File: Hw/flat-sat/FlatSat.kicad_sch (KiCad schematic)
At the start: 84 parts, among them J1 Antenna, J2 Antenna, J3 periphs, J4 SWD, P1 USB_C_Plug_USB2.0, U1 TLV75733PDBVR, U10 LIS2DH, U11 BME280 /BMP280, U2 0900FM15D0039, U3 PE42421, U4 SX1262IMLTRT, U5 W25Q16JV, U6 0900FM15D0039, U7 PE42421, U8 SX1262IMLTRT, U9 RP2040, Y1 32Mhz, Y2 32Mhz, Y3 12MHz

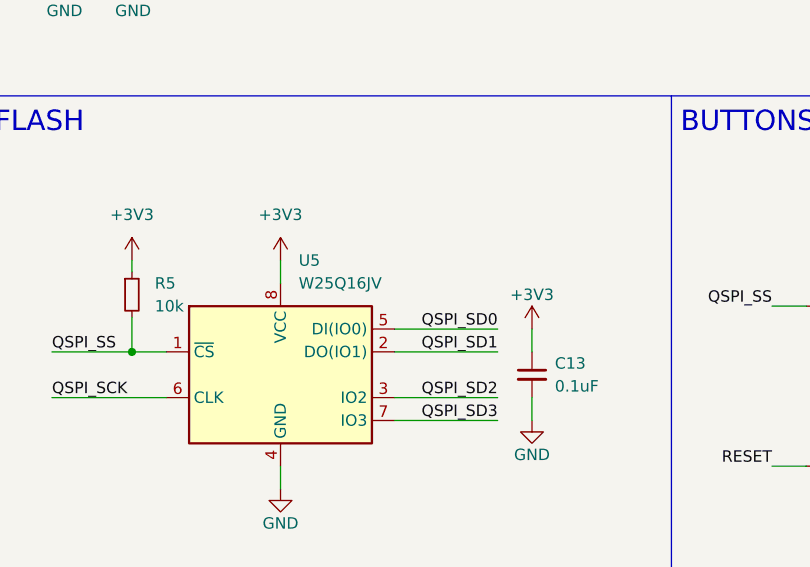
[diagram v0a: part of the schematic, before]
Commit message: feat(Hw):Update_Bom
#part memory flash updated
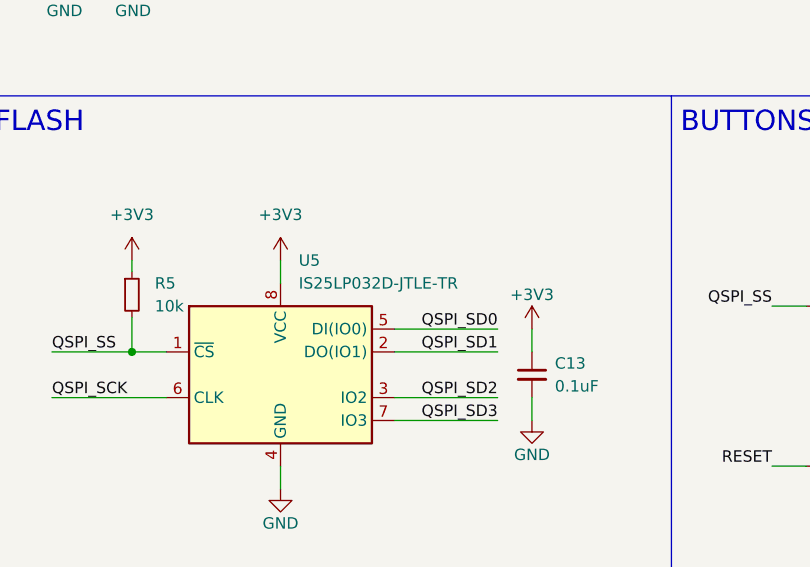
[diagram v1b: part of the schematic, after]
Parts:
- U5: value W25Q16JV -> IS25LP032D-JTLE-TR; LCSC# C571259 -> C5119926; Mouser# 454-W25Q16JVUUIQTR -> (none); manf# W25Q16JVUUIQ TR -> IS25LP032D-JTLE-TR; provedor Mouser -> LCSC
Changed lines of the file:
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@@
 			)
 		)
-		(property "Value" "W25Q16JV"
+		(property "Value" "IS25LP032D-JTLE-TR"
 			(at 46.4694 104.14 0)
 			(effects
@@
 			)
 		)
-		(property "Mouser#" "454-W25Q16JVUUIQTR"
+		(property "Mouser#" ""
 			(at 44.45 114.3 0)
 			(effects
@@
 			)
 		)
-		(property "manf#" "W25Q16JVUUIQ TR"
+		(property "manf#" "IS25LP032D-JTLE-TR"
 			(at 44.45 114.3 0)
 			(effects
@@
 			)
 		)
-		(property "provedor" "Mouser"
+		(property "provedor" "LCSC"
 			(at 44.45 114.3 0)
 			(effects
@@
 			)
 		)
-		(property "LCSC#" "C571259"
+		(property "LCSC#" "C5119926"
 			(at 44.45 114.3 0)
 			(effects
